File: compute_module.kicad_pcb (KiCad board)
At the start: 4 copper layers, 93.2 x 62.4 mm, 53 parts, among them J1 2001-1-2-21-00-BK, P1 POWER, P2 HOST, P3 CAM1, P4 CONN_02X20, Q1 2N7002P.215, Q2 DMP3056L-7, Q3 2N7002P.215, U1 REG1117-3.3, U3 REG1117A-1.8

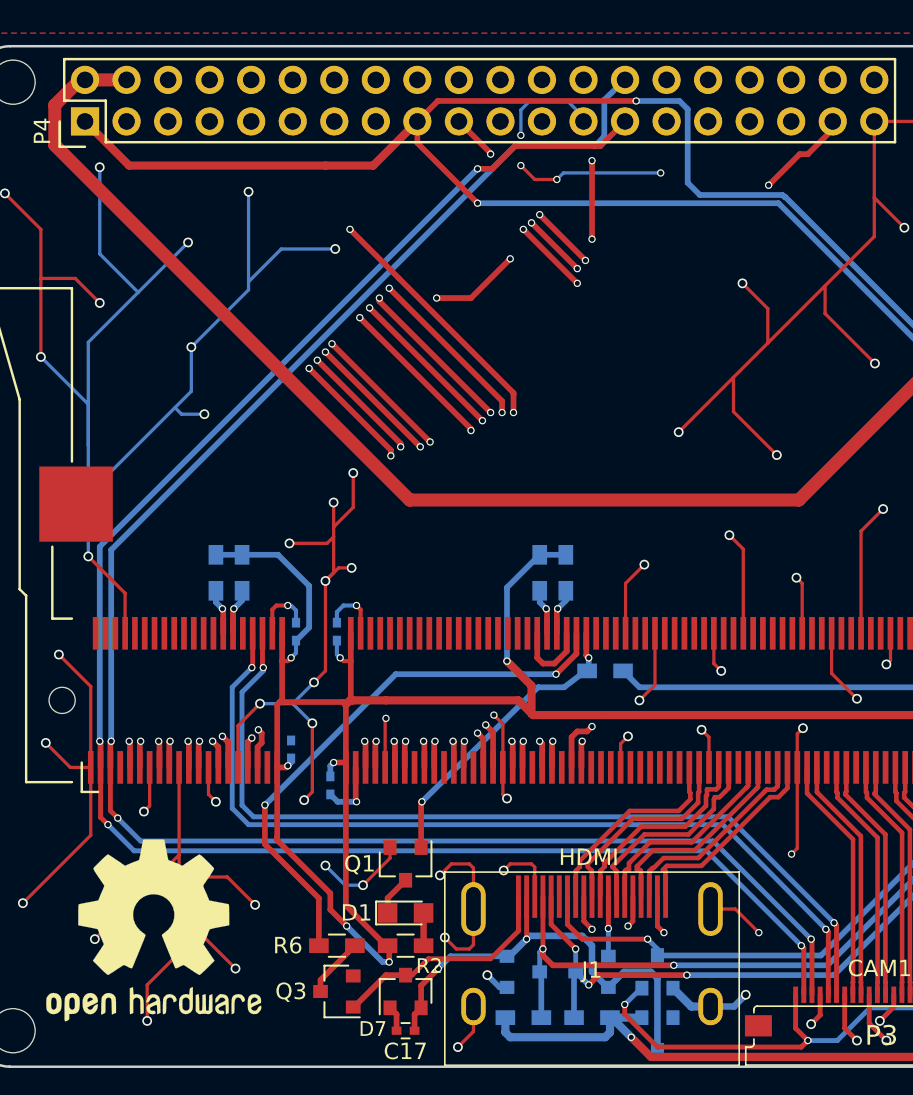
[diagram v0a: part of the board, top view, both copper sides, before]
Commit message: Moved camera sda and scl to gpio 28 and 29
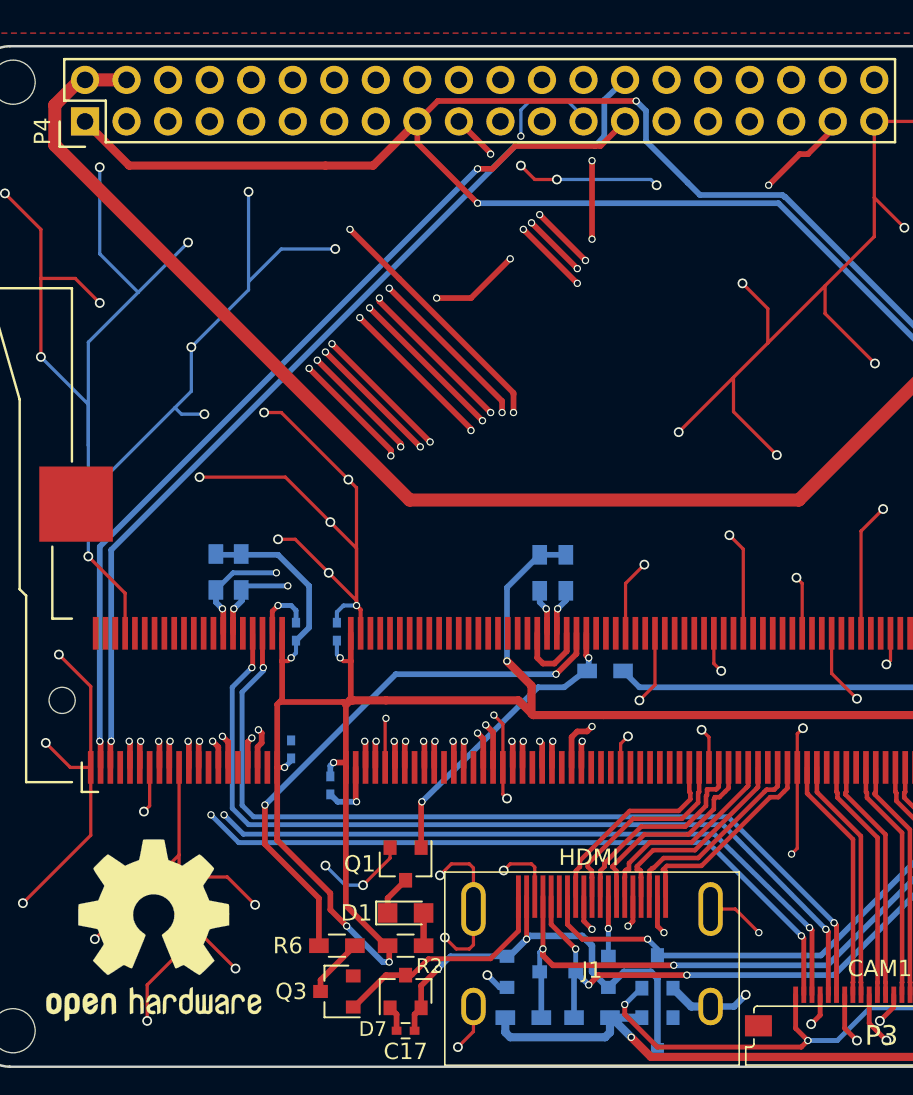
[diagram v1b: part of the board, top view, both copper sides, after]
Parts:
- R10, R9: value 10K -> 1.8K
- moved R9 1.60 mm to (102.2, 76.2)
- moved R10 1.55 mm to (103.8, 76.2)
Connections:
- MD1 pad 28: GPIO28 -> CD1_SDA
- MD1 pad 3: CD1_SDA -> GPIO0
- MD1 pad 30: GPIO29 -> CD1_SCL
- MD1 pad 5: CD1_SCL -> GPIO1
- P4 pad 27: CD1_SDA -> GPIO0
- P4 pad 28: CD1_SCL -> GPIO1
- R10 pad 2: GPIO28 -> CD1_SCL
- R9 pad 2: GPIO29 -> CD1_SDA
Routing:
- net GPIO1: track 0.00 -> 57.9 mm, vias 0 -> 1
- net GPIO0: track 0.00 -> 56.4 mm, vias 0 -> 2
- net CD1_SCL: track 110.1 -> 67.3 mm, vias 3 -> 4
- net CD1_SDA: track 108.6 -> 69.5 mm
- net GPIO29: track 2.83 -> 0.00 mm, vias 1 -> 0
- net GPIO28: track 2.79 -> 0.00 mm, vias 1 -> 0
- net +3V3: track 362.7 -> 361.1 mm
- net GND: track 684.9 -> 683.6 mm, vias 124 -> 120

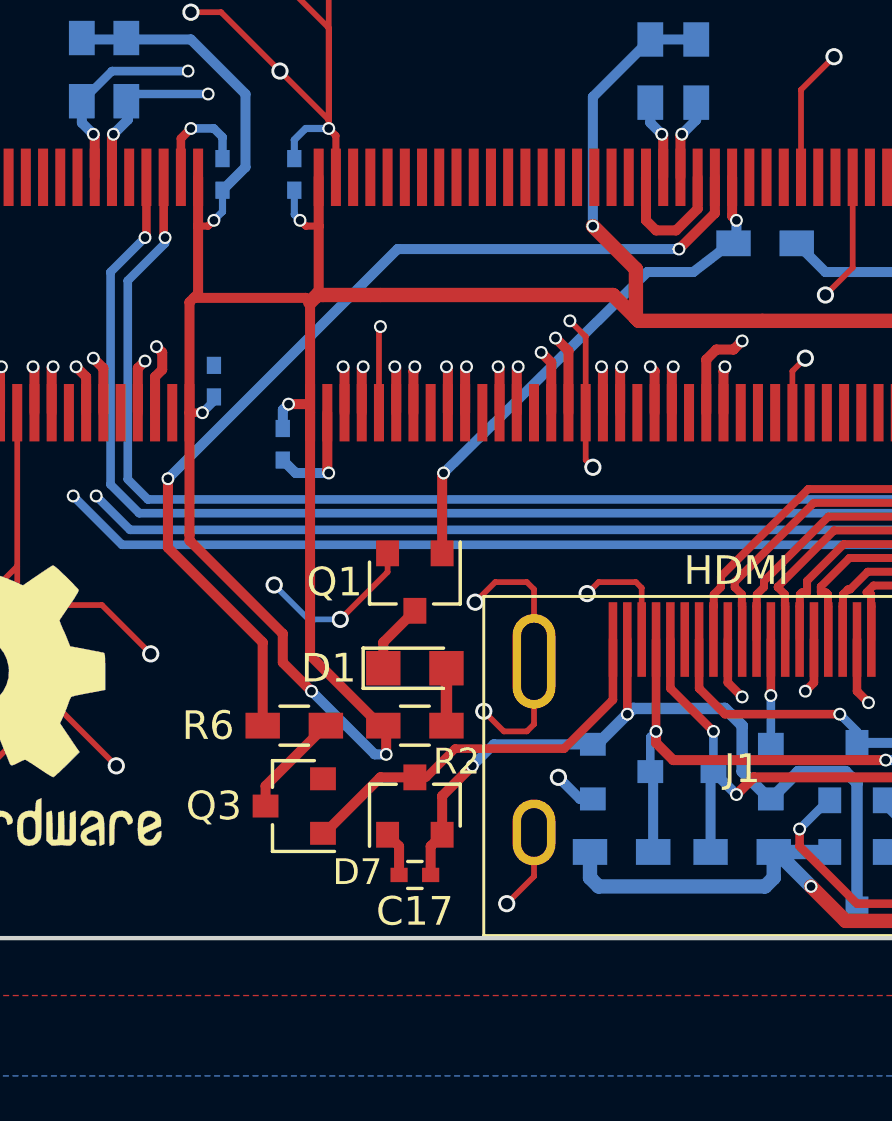
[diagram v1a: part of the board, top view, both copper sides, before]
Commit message: Added power LED
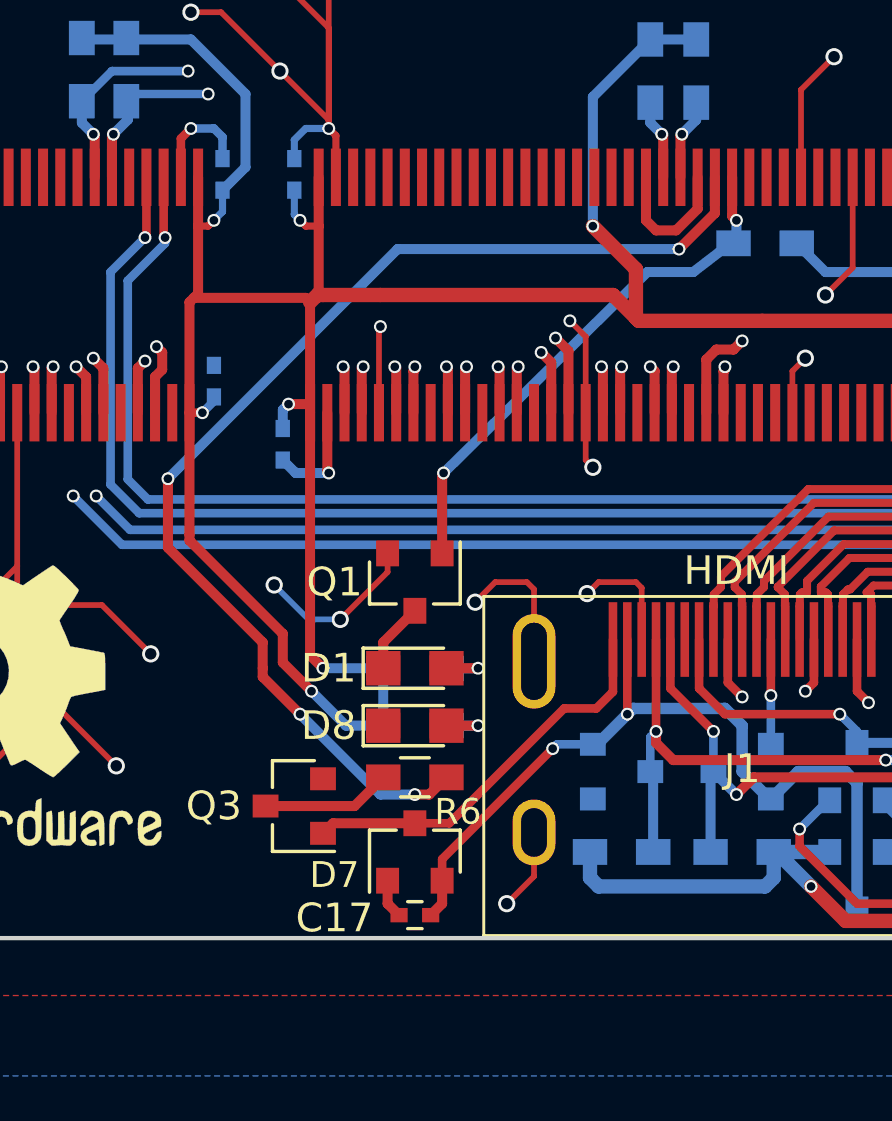
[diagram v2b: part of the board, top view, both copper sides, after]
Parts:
- added D8: LED, LEDs:LED_0805, F.Cu at (113.8, 99.0)
- added R11: 1K, Resistors_SMD:R_0603_HandSoldering, B.Cu at (113.8, 99.0)
- R2: moved to B.Cu
- R7, R8: value 10K -> 100K
- moved R6 4.57 mm to (113.8, 100.8), turned to 180 degrees
- moved R2 2.00 mm to (113.8, 97.0)
- moved D7 1.60 mm to (113.8, 103.4)
- moved C17 1.40 mm to (113.8, 105.6)
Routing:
- net HDMI_HPD_N_1V8: track 34.1 -> 40.7 mm, vias 2 -> 4
- net GND: track 683.6 -> 677.6 mm, vias 120 -> 118
- net Net-(D8-Pad2): track 0.00 -> 2.20 mm, vias 0 -> 1
- net Net-(Q3-Pad3): track 3.67 -> 4.51 mm
- net Net-(D1-Pad2): track 2.00 -> 2.20 mm, vias 0 -> 1

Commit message: Minor fixes
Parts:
- moved C8 0.10 mm to (159.1, 79.8)
- turned R7 to 90 degrees
- turned R8 to 90 degrees
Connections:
- R7 pad 1: +3V3 -> GPIO45
- R7 pad 2: GPIO45 -> GND
- R8 pad 1: +3V3 -> GPIO44
- R8 pad 2: GPIO44 -> GND
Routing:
- net +3V3: track 360.7 -> 348.0 mm, vias 18 -> 17
- net GND: track 677.6 -> 678.5 mm
- net +5V: track 245.5 -> 245.7 mm, vias 8 -> 7

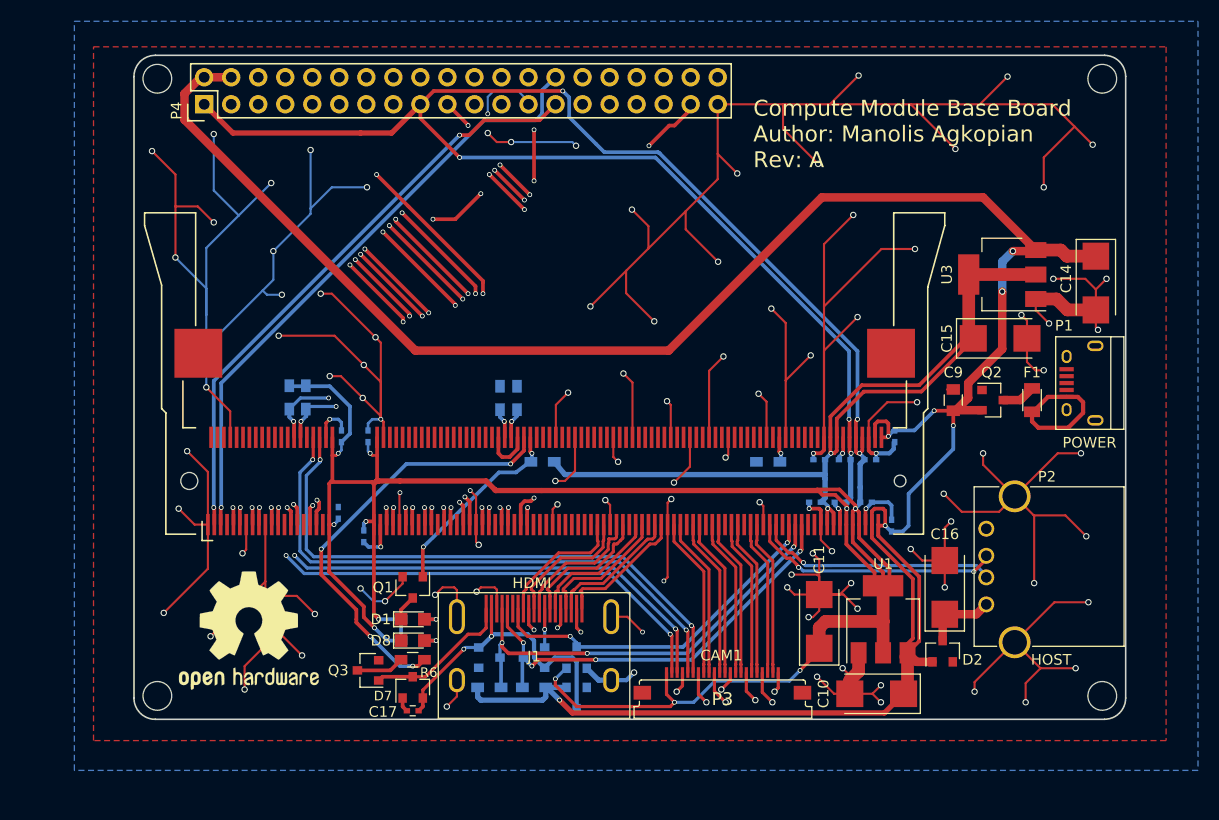
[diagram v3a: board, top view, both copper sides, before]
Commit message: Added audio jack
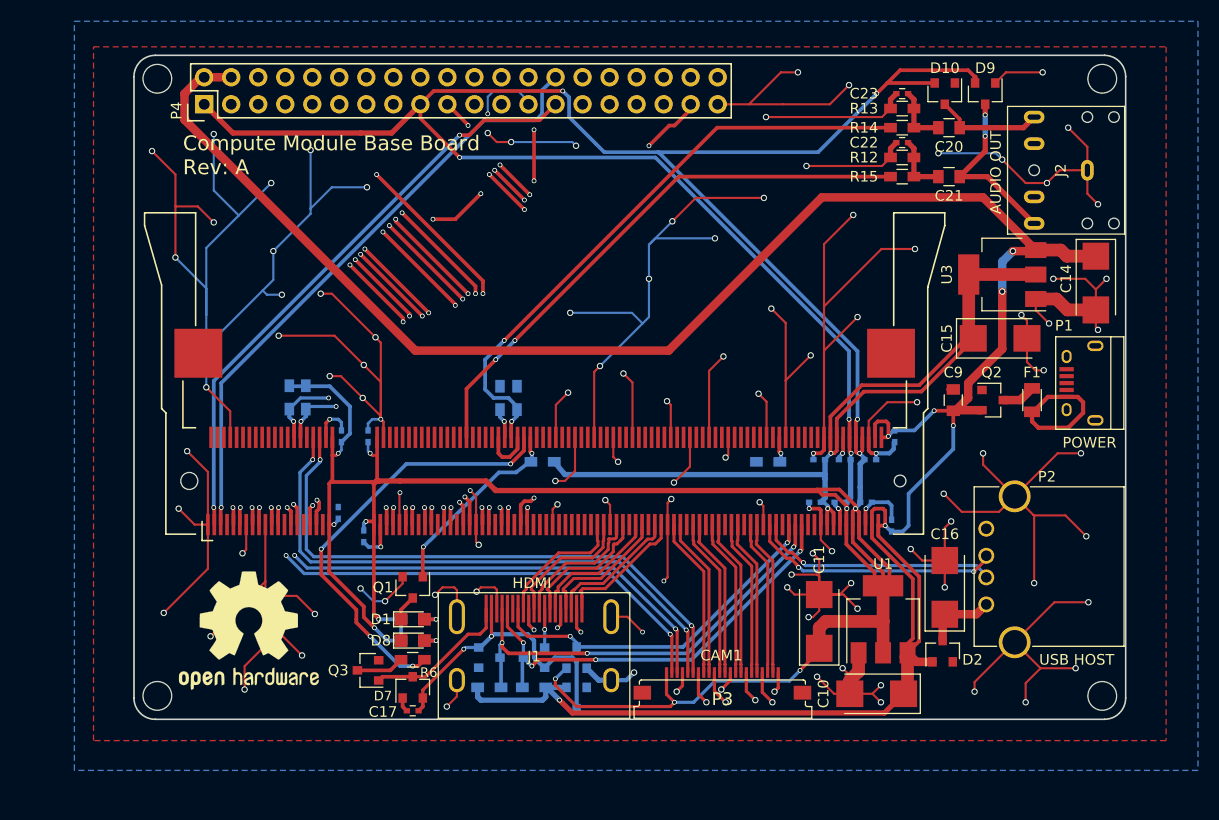
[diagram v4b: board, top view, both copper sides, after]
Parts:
- added C20: 10uF, Capacitors_SMD:C_0805, F.Cu at (164.2, 50.8)
- added C21: 10uF, Capacitors_SMD:C_0805, F.Cu at (164.2, 55.4)
- added C22: 33nF, Capacitors_SMD:C_0402, F.Cu at (159.8, 52.2)
- added C23: 33nF, Capacitors_SMD:C_0402, F.Cu at (159.8, 47.6)
- added D10: BAV99, TO_SOT_Packages_SMD:SOT-23, F.Cu at (163.8, 47.6)
- added D9: BAV99, TO_SOT_Packages_SMD:SOT-23, F.Cu at (167.6, 47.6)
- added J2: JC-128, jc-128:JC-128, F.Cu at (177.2, 54.8)
- added R12: 150R, Resistors_SMD:R_0603_HandSoldering, F.Cu at (159.8, 53.6)
- added R13: 150R, Resistors_SMD:R_0603_HandSoldering, F.Cu at (159.8, 49.0)
- added R14: 270R, Resistors_SMD:R_0603_HandSoldering, F.Cu at (159.8, 50.8)
- added R15: 270R, Resistors_SMD:R_0603_HandSoldering, F.Cu at (159.8, 55.4)
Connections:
- MD1 pad 70: Net-(MD1-Pad70) -> GPIO40
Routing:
- net GPIO45: track 2.83 -> 56.7 mm, vias 1 -> 2
- net GPIO40: track 0.00 -> 52.7 mm, vias 0 -> 2
- net +3V3: track 348.0 -> 386.3 mm, vias 17 -> 18
- net Net-(C21-Pad2): track 0.00 -> 16.6 mm, vias 0 -> 2
- net GND: track 678.5 -> 689.6 mm, vias 118 -> 123
- net Net-(C20-Pad2): track 0.00 -> 10.2 mm
- net Net-(C21-Pad1): track 0.00 -> 5.73 mm
- net Net-(C20-Pad1): track 0.00 -> 5.73 mm
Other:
- board text added: "AUDIO OUT"
- board text added: "Compute Module Base Board Rev: A"
- board text added: "USB HOST"
- board text removed: "Compute Module Base Board Author: Manolis Agkopian Rev: A"
- board text removed: "HOST"

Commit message: Cleaned up libs
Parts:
- MD1: footprint footprints:Conn_TE-DDR2-SODIMM-0.6-200P-doublesided -> Conn_TE-DDR2-SODIMM:Conn_TE-DDR2-SODIMM-0.6-200P-doublesided

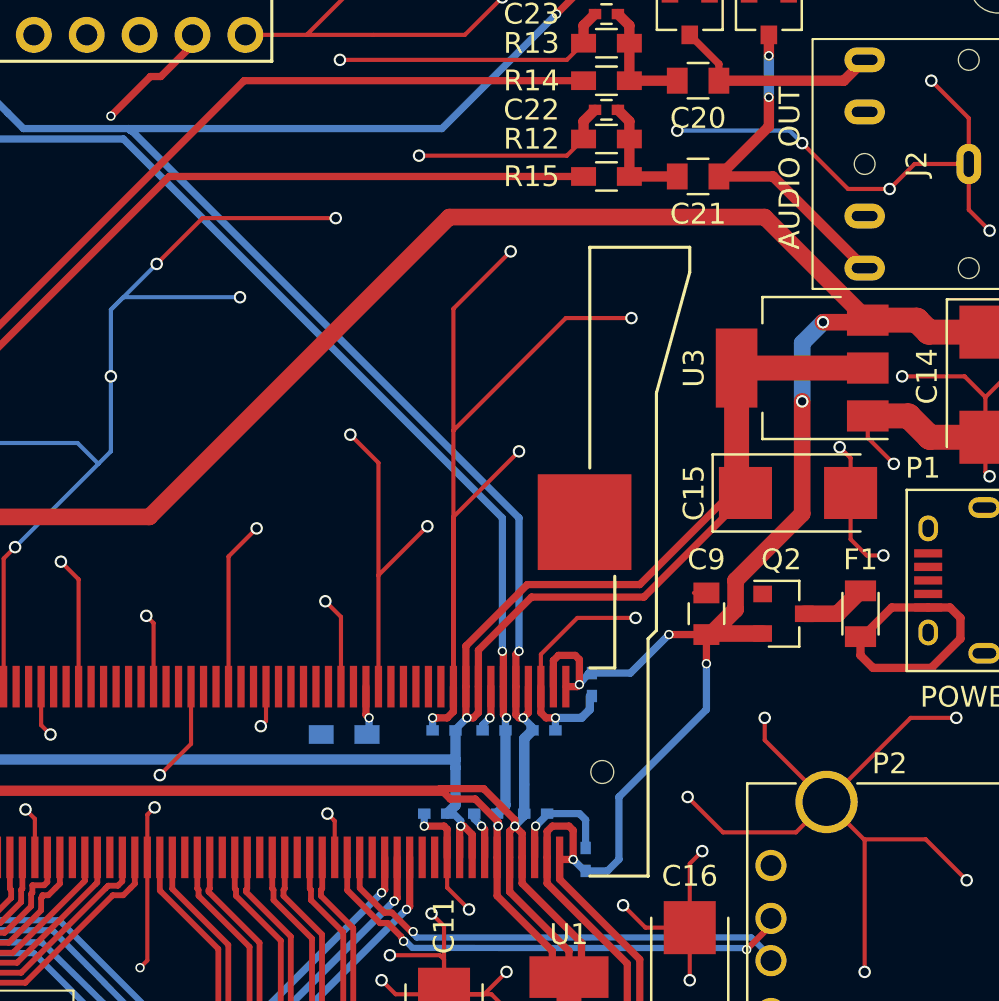
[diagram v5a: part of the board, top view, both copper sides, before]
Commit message: Replaced 1uF input cap with 100nF
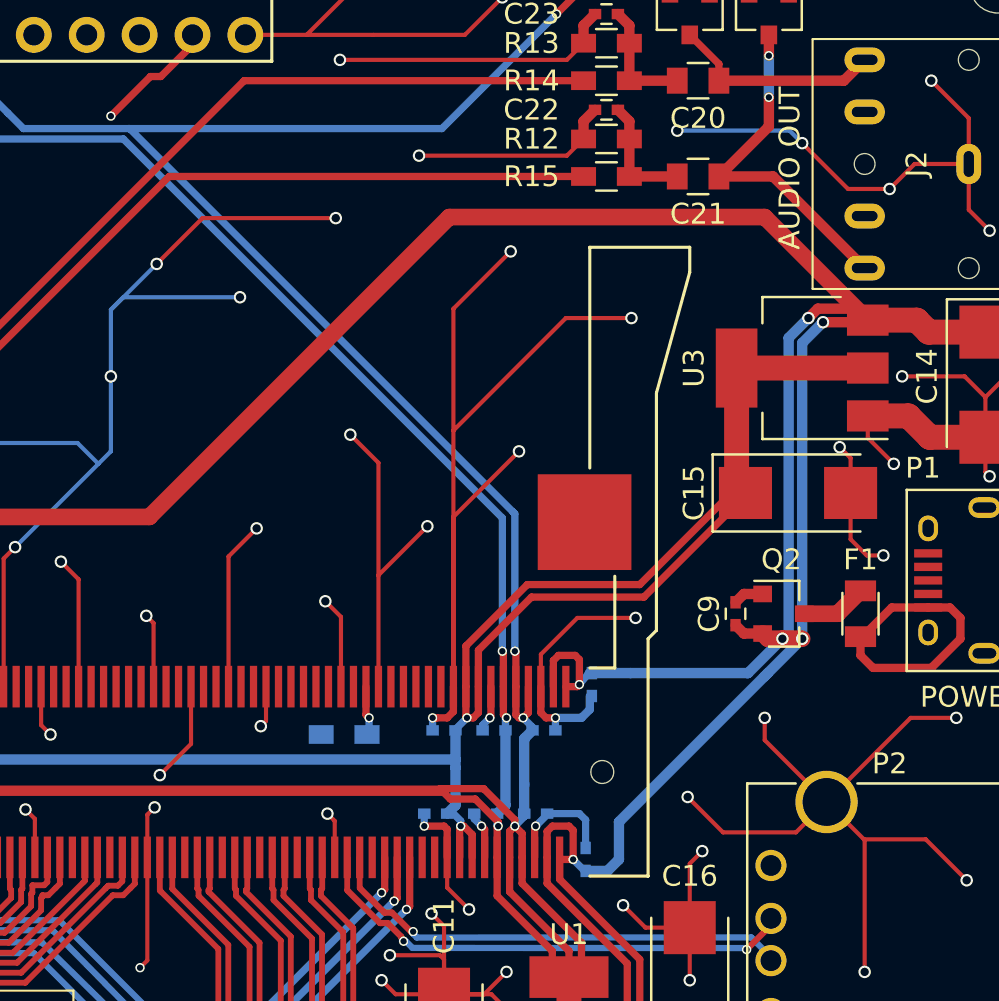
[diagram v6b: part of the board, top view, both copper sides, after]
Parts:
- C9: value 1uF -> 100nF; footprint Capacitors_SMD:C_0805 -> Capacitors_SMD:C_0402
- D1: value LED -> GREEN LED
- D8: value LED -> RED LED
- moved C9 1.40 mm to (166.0, 76.4)
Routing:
- net +5V: track 245.7 -> 270.5 mm
- net GND: track 689.6 -> 690.4 mm
